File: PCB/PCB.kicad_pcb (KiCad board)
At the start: 2 copper layers, 68.6 x 53.3 mm, 17 parts, among them J1 Conn_01x04_Male, P1 Power, P2 Analog, P3 Digital, P4 Digital, P5 CONN_01X01, P6 CONN_01X01, P7 CONN_01X01, P8 CONN_01X01, U1 LM393

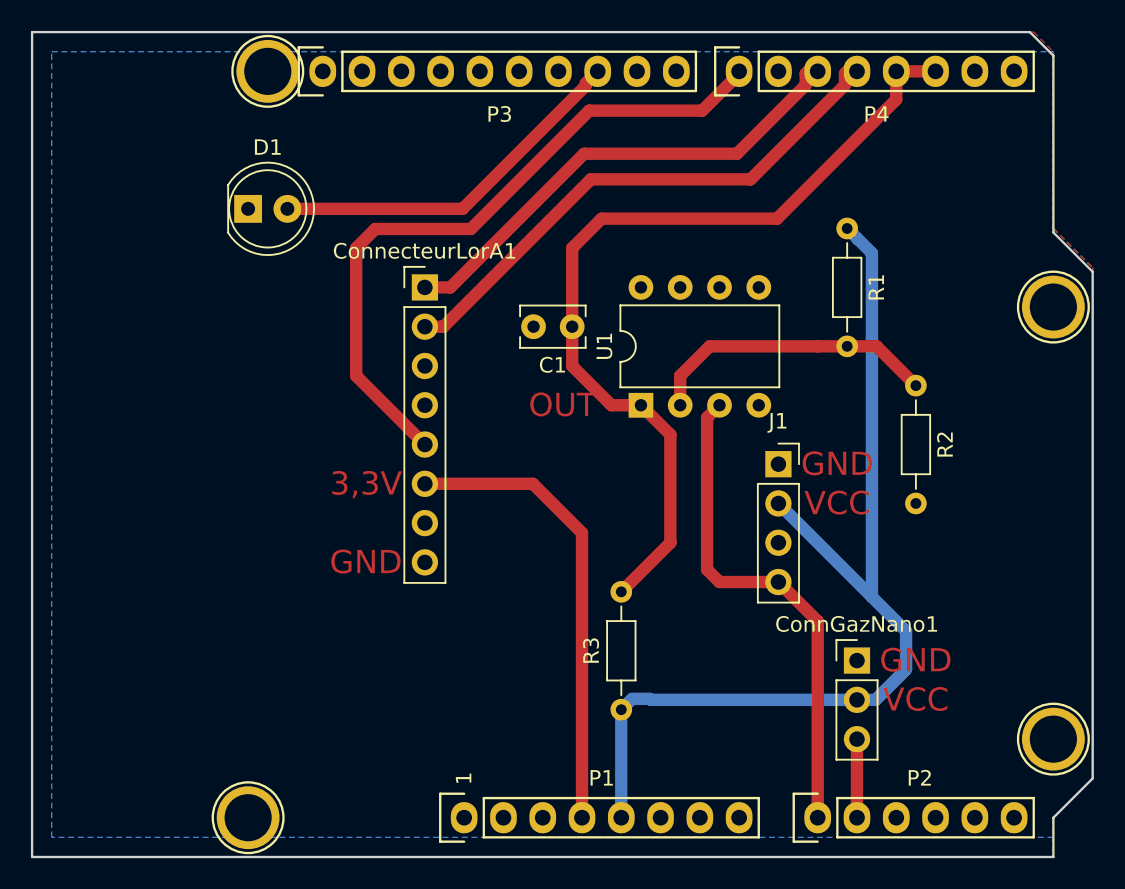
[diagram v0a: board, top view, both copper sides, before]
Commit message: ajout pcb capteur nano et maj pcb shield
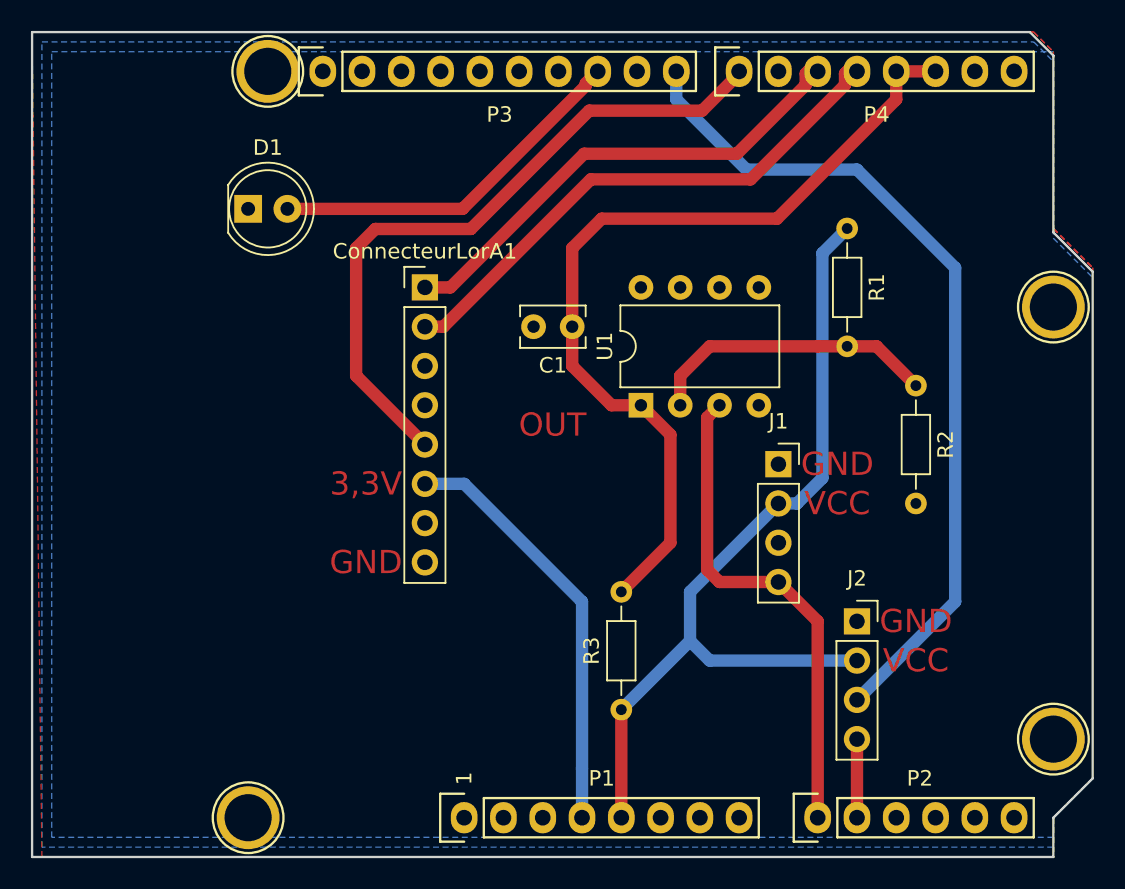
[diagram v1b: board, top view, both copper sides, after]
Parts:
- removed ConnGazNano1: Conn_01x03_Male, Connector_PinHeader_2.54mm:PinHeader_1x03_P2.54mm_Vertical
- added J2: Conn_01x04_Male, Connector_PinSocket_2.54mm:PinSocket_1x04_P2.54mm_Vertical, F.Cu at (164.3, 111.1)
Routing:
- net /8: track 0.00 -> 54.9 mm
- net +5V: track 66.5 -> 56.3 mm
- net +3V3: track 29.9 -> 27.3 mm
